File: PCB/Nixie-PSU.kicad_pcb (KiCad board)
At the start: 2 copper layers, 76.2 x 50.8 mm, 17 parts, among them J1 Conn_Mains, J2 Conn_Pwr_Out, Q1 MJE18008-D

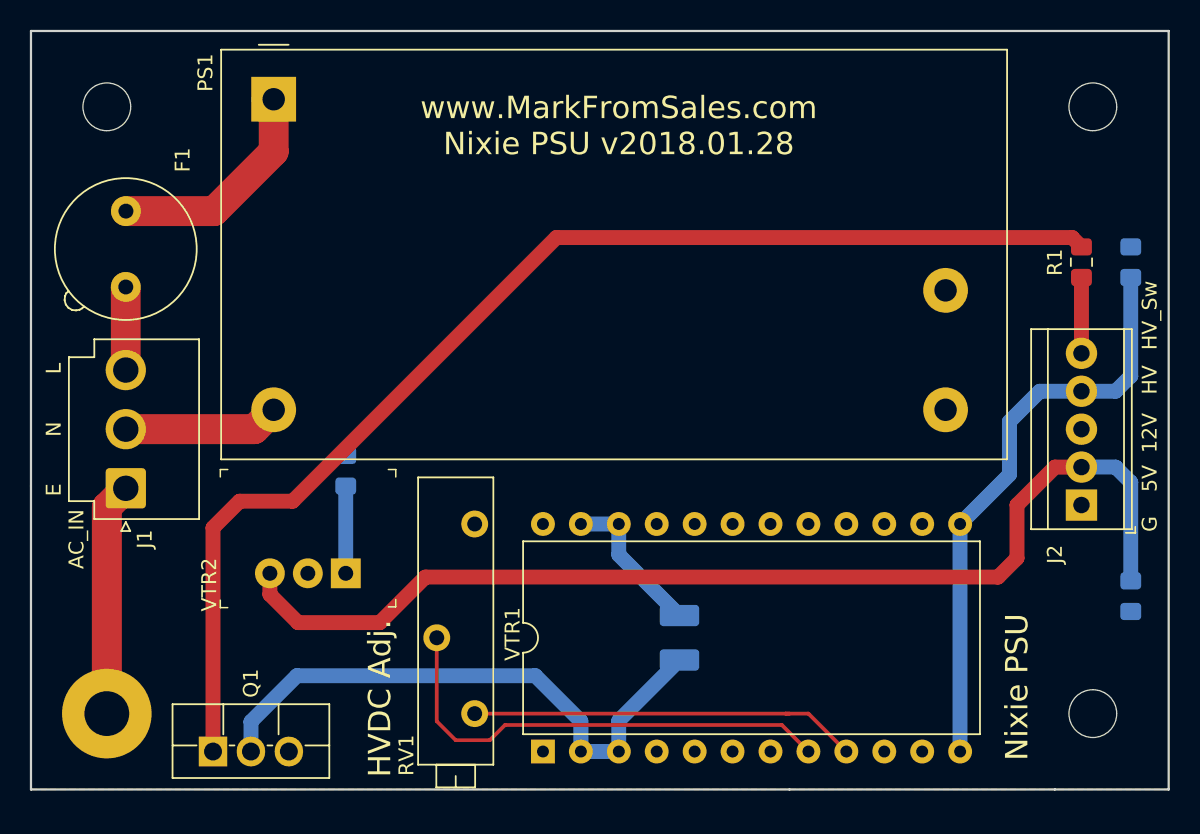
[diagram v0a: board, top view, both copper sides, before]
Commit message: Rounded Corners
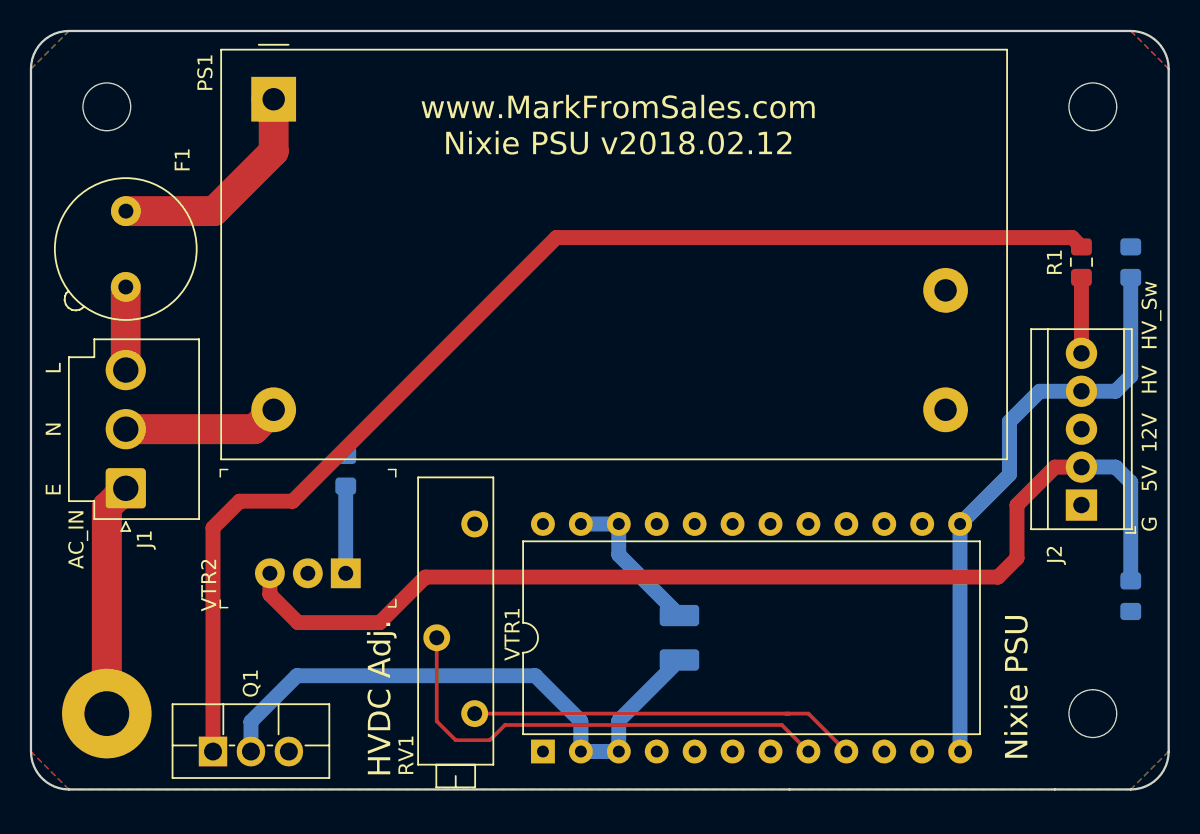
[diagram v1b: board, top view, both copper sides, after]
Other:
- outline, holes or cut-outs redrawn
- board text added: "www.MarkFromSales.com Nixie PSU v2018.02.12"
- board text removed: "www.MarkFromSales.com Nixie PSU v2018.01.28"
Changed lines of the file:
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@@
   (general
     (thickness 1.6)
-    (drawings 20)
+    (drawings 24)
     (tracks 59)
     (zones 0)
@@
   )
   (setup
-    (last_trace_width 2)
+    (last_trace_width 1)
     (user_trace_width 2)
     (trace_clearance 0.4)
@@
     (tags "mounting hole 3mm")
     (attr virtual)
-    (fp_text reference H1 (at 0 -4) (layer F.SilkS) hide
+    (fp_text reference H1 (at 0 0) (layer F.SilkS) hide
       (effects (font (size 1 1) (thickness 0.15)))
     )
@@
     (tags "mounting hole 3.2mm no annular m3")
     (attr virtual)
-    (fp_text reference H2 (at 0 -4.2 90) (layer F.SilkS) hide
+    (fp_text reference H2 (at 0 0 180) (layer F.SilkS) hide
       (effects (font (size 1 1) (thickness 0.15)))
     )
@@
     (tags "mounting hole 3.2mm no annular m3")
     (attr virtual)
-    (fp_text reference H3 (at 0 -4.2) (layer F.SilkS) hide
+    (fp_text reference H3 (at 0 0) (layer F.SilkS) hide
       (effects (font (size 1 1) (thickness 0.15)))
     )
@@
     (tags "mounting hole 3.2mm no annular m3")
     (attr virtual)
-    (fp_text reference H4 (at 0 -4.2) (layer F.SilkS) hide
+    (fp_text reference H4 (at 0 0) (layer F.SilkS) hide
       (effects (font (size 1 1) (thickness 0.15)))
     )
@@
     (pad 1 np_thru_hole circle (at 0 0) (size 3.2 3.2) (drill 3.2) (layers *.Cu *.Mask))
   )
+  (gr_arc (start 162.56 53.34) (end 165.1 53.34) (angle -90) (layer Edge.Cuts) (width 0.15))
+  (gr_arc (start 162.56 99.06) (end 162.56 101.6) (angle -90) (layer Edge.Cuts) (width 0.15))
+  (gr_arc (start 91.44 99.06) (end 88.9 99.06) (angle -90) (layer Edge.Cuts) (width 0.15))
+  (gr_arc (start 91.44 53.34) (end 91.44 50.8) (angle -90) (layer Edge.Cuts) (width 0.15))
   (gr_text E (at 90.424 81.534 90) (layer F.SilkS)
     (effects (font (size 1 1) (thickness 0.15)))
@@
     (effects (font (size 1 1) (thickness 0.15)))
   )
-  (gr_text "www.MarkFromSales.com\nNixie PSU v2018.01.28" (at 128.27 57.15) (layer B.SilkS)
+  (gr_text "www.MarkFromSales.com\nNixie PSU v2018.02.12" (at 128.27 57.15) (layer B.SilkS)
     (effects (font (size 1.5 1.5) (thickness 0.3)) (justify mirror))
   )
-  (gr_text "www.MarkFromSales.com\nNixie PSU v2018.01.28" (at 128.27 57.15) (layer F.SilkS)
+  (gr_text "www.MarkFromSales.com\nNixie PSU v2018.02.12" (at 128.27 57.15) (layer F.SilkS)
     (effects (font (size 1.5 1.5) (thickness 0.3)))
   )
-  (gr_line (start 165.1 50.8) (end 88.9 50.8) (layer Edge.Cuts) (width 0.15))
-  (gr_line (start 165.1 101.6) (end 165.1 50.8) (layer Edge.Cuts) (width 0.15))
-  (gr_line (start 157.48 101.6) (end 165.1 101.6) (layer Edge.Cuts) (width 0.15))
+  (gr_line (start 162.56 50.8) (end 91.44 50.8) (layer Edge.Cuts) (width 0.15))
+  (gr_line (start 165.1 99.06) (end 165.1 53.34) (layer Edge.Cuts) (width 0.15))
+  (gr_line (start 157.48 101.6) (end 162.56 101.6) (layer Edge.Cuts) (width 0.15))
   (gr_line (start 139.7 101.6) (end 157.48 101.6) (layer Edge.Cuts) (width 0.15))
-  (gr_line (start 88.9 101.6) (end 139.7 101.6) (layer Edge.Cuts) (width 0.15))
-  (gr_line (start 88.9 81.28) (end 88.9 101.6) (layer Edge.Cuts) (width 0.15))
-  (gr_line (start 88.9 50.8) (end 88.9 81.28) (layer Edge.Cuts) (width 0.15))
+  (gr_line (start 91.44 101.6) (end 139.7 101.6) (layer Edge.Cuts) (width 0.15))
+  (gr_line (start 88.9 81.28) (end 88.9 99.06) (layer Edge.Cuts) (width 0.15))
+  (gr_line (start 88.9 53.34) (end 88.9 81.28) (layer Edge.Cuts) (width 0.15))
   (segment (start 150.128 76.2) (end 150.156 76.172) (width 1) (layer B.Cu) (net 1) (status 30))
-  (segment (start 151.13 99.06) (end 151.13 83.82) (width 1) (layer B.Cu) (net 4) (status 30))
   (segment (start 125.73 83.82) (end 128.27 83.82) (width 1) (layer B.Cu) (net 2) (status 30))
   (segment (start 128.27 85.8885) (end 132.334 89.9525) (width 1) (layer B.Cu) (net 2) (status 20))
@@
   (segment (start 153.67 87.376) (end 115.316 87.376) (width 1) (layer F.Cu) (net 3))
   (segment (start 115.316 87.376) (end 112.268 90.424) (width 1) (layer F.Cu) (net 3))
+  (segment (start 151.13 99.06) (end 151.13 83.82) (width 1) (layer B.Cu) (net 4) (status 30))
   (segment (start 162.56 73.914) (end 162.56 67.31) (width 1) (layer B.Cu) (net 4) (status 20))
   (segment (start 159.258 74.93) (end 161.544 74.93) (width 1) (layer B.Cu) (net 4) (status 10))
@@
     (polygon
       (pts
-        (xy 88.9 50.8) (xy 88.9 101.6) (xy 165.1 101.6) (xy 165.1 50.8)
+        (xy 162.56 101.6) (xy 91.44 101.6) (xy 88.9 99.06) (xy 88.9 53.34) (xy 91.44 50.8)
+        (xy 162.56 50.8) (xy 165.1 53.34) (xy 165.1 99.06)
       )
     )
@@
     (polygon
       (pts
-        (xy 88.9 50.8) (xy 88.9 101.6) (xy 165.1 101.6) (xy 165.1 50.8)
+        (xy 162.56 101.6) (xy 91.44 101.6) (xy 88.9 99.06) (xy 88.9 53.34) (xy 91.44 50.8)
+        (xy 162.56 50.8) (xy 165.1 53.34) (xy 165.1 99.06)
       )
     )
